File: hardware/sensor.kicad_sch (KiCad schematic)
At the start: 0 parts

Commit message: Alpha 1.0.0 Schematic
First Schematic Version for initial checkup
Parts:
- added C? (x3): 10nF, symbol Device:C
- added C? (x3): 100nF, symbol Device:C
- added R? (x3): 47k, symbol Device:R
- added R? (x3): 91k, symbol Device:R
- added U? (x3): LM321, Package_TO_SOT_SMD:SOT-23-5, symbol Amplifier_Operational:LM321
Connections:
- net 1: now also C?.1, R?.2
- net 2: now also C?.1, R?.2
- net 3: now also C?.1, R?.2
- new net: R?.1, R?.2, U?.1 (+) (x3)
- new net +3V3: C?.1, C?.1, C?.1, U?.5 (V+), U?.5 (V+), U?.5 (V+)
- new net GND: C?.2, C?.2, C?.2, C?.2, C?.2, C?.2, R?.1, R?.1, R?.1, U?.2 (V-), U?.2 (V-), U?.2 (V-), U?.3 (-), U?.3 (-), U?.3 (-), U?.4, U?.4, U?.4
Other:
- note added: "5V to 3V3 signal scaling, noise reduction and Voltage Follower"

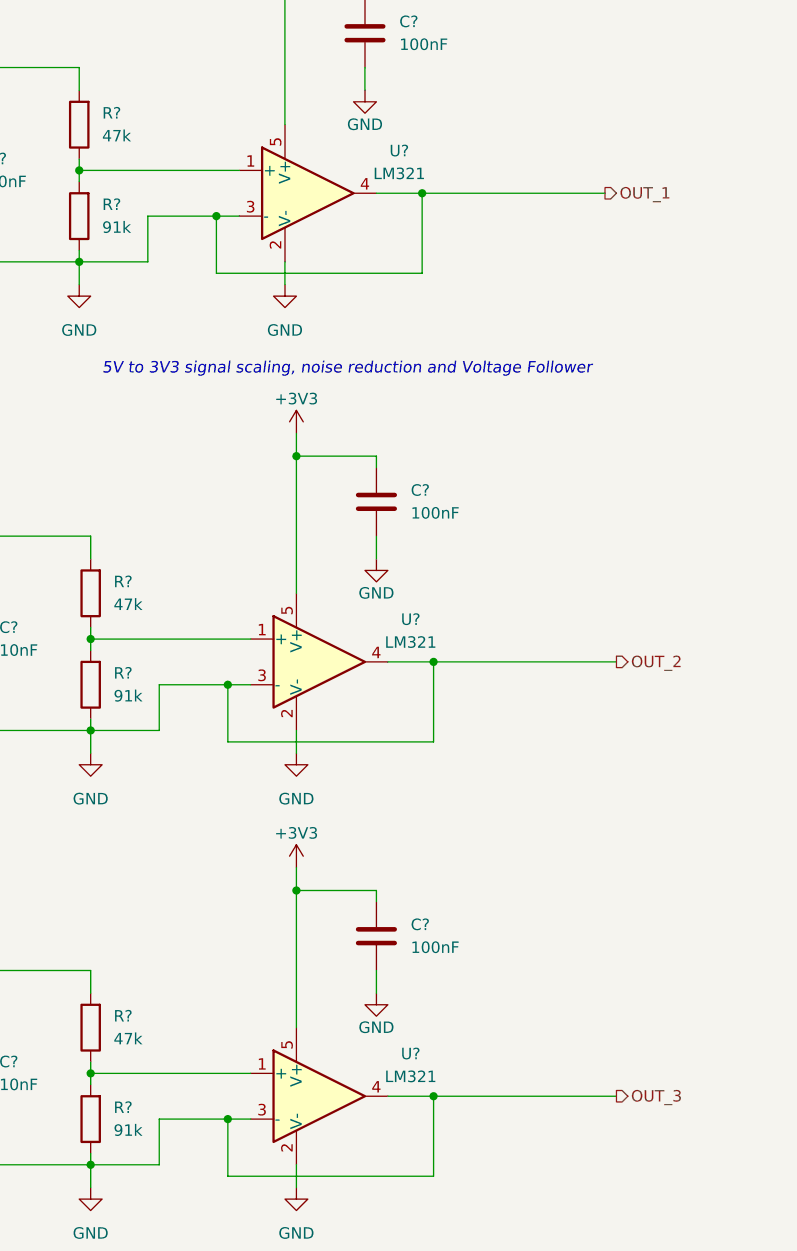
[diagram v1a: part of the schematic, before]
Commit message: Minor changes on v1 schematic
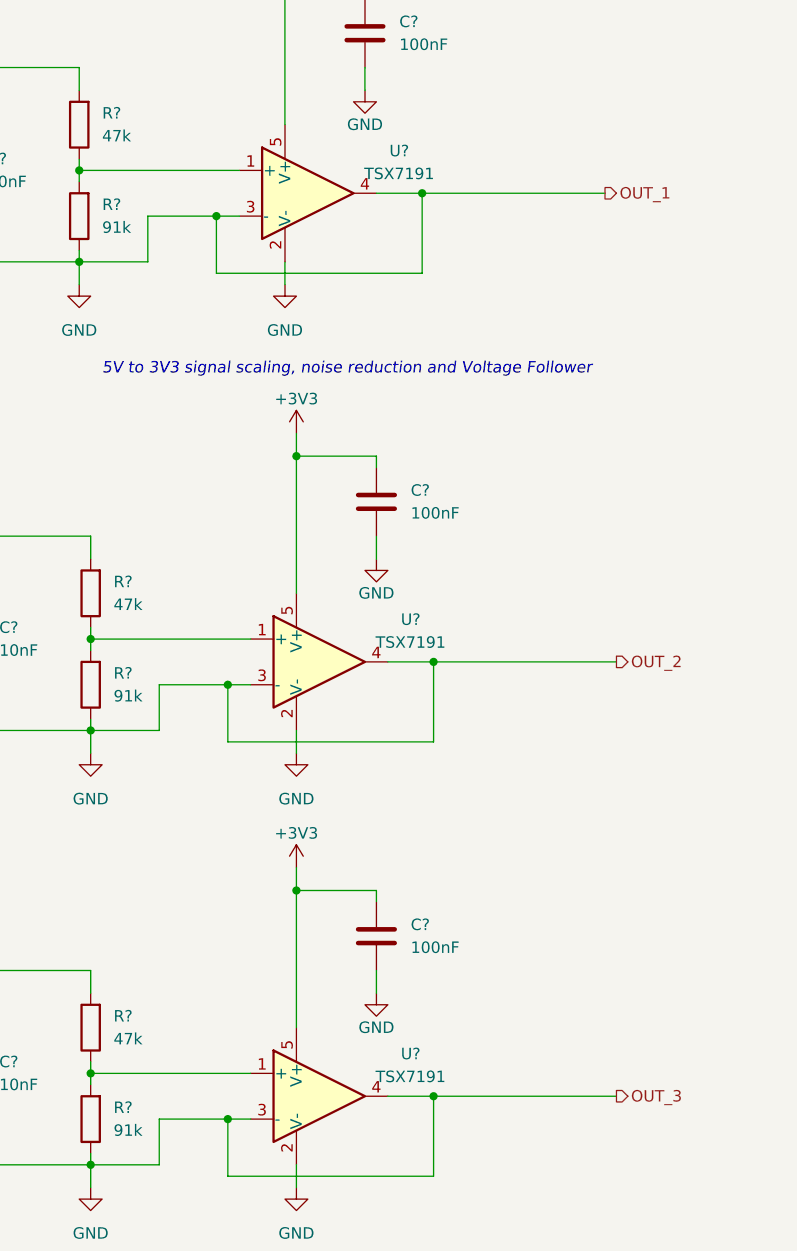
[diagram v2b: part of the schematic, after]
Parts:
- U? (x3): value LM321 -> TSX7191; footprint Package_TO_SOT_SMD:SOT-23-5 -> (none)
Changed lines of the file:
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@@
     (in_bom yes) (on_board yes) (fields_autoplaced)
     (property "Reference" "U?" (id 0) (at 157.48 52.451 0))
-    (property "Value" "LM321" (id 1) (at 157.48 54.991 0))
-    (property "Footprint" "Package_TO_SOT_SMD:SOT-23-5" (id 2) (at 147.32 57.15 0)
-      (effects (font (size 1.27 1.27)) hide)
-    )
-    (property "Datasheet" "http://www.ti.com/lit/ds/symlink/lm321.pdf" (id 3) (at 147.32 57.15 0)
+    (property "Value" "TSX7191" (id 1) (at 157.48 54.991 0))
+    (property "Footprint" "" (id 2) (at 147.32 57.15 0)
+      (effects (font (size 1.27 1.27)) hide)
+    )
+    (property "Datasheet" "" (id 3) (at 147.32 57.15 0)
       (effects (font (size 1.27 1.27)) hide)
     )
@@
     (in_bom yes) (on_board yes) (fields_autoplaced)
     (property "Reference" "U?" (id 0) (at 158.75 104.521 0))
-    (property "Value" "LM321" (id 1) (at 158.75 107.061 0))
-    (property "Footprint" "Package_TO_SOT_SMD:SOT-23-5" (id 2) (at 148.59 109.22 0)
-      (effects (font (size 1.27 1.27)) hide)
-    )
-    (property "Datasheet" "http://www.ti.com/lit/ds/symlink/lm321.pdf" (id 3) (at 148.59 109.22 0)
+    (property "Value" "TSX7191" (id 1) (at 158.75 107.061 0))
+    (property "Footprint" "" (id 2) (at 148.59 109.22 0)
+      (effects (font (size 1.27 1.27)) hide)
+    )
+    (property "Datasheet" "" (id 3) (at 148.59 109.22 0)
       (effects (font (size 1.27 1.27)) hide)
     )
@@
     (in_bom yes) (on_board yes) (fields_autoplaced)
     (property "Reference" "U?" (id 0) (at 158.75 152.781 0))
-    (property "Value" "LM321" (id 1) (at 158.75 155.321 0))
-    (property "Footprint" "Package_TO_SOT_SMD:SOT-23-5" (id 2) (at 148.59 157.48 0)
-      (effects (font (size 1.27 1.27)) hide)
-    )
-    (property "Datasheet" "http://www.ti.com/lit/ds/symlink/lm321.pdf" (id 3) (at 148.59 157.48 0)
-      (effects (font (size 1.27 1.27)) hide)
-    )
+    (property "Value" "TSX7191" (id 1) (at 158.75 155.321 0))
+    (property "Footprint" "" (id 2) (at 148.59 157.48 0)
+      (effects (font (size 1.27 1.27)) hide)
+    )
+    (property "Datasheet" "" (id 3) (at 148.59 157.48 0)
+      (effects (font (size 1.27 1.27)) hide)
+    )

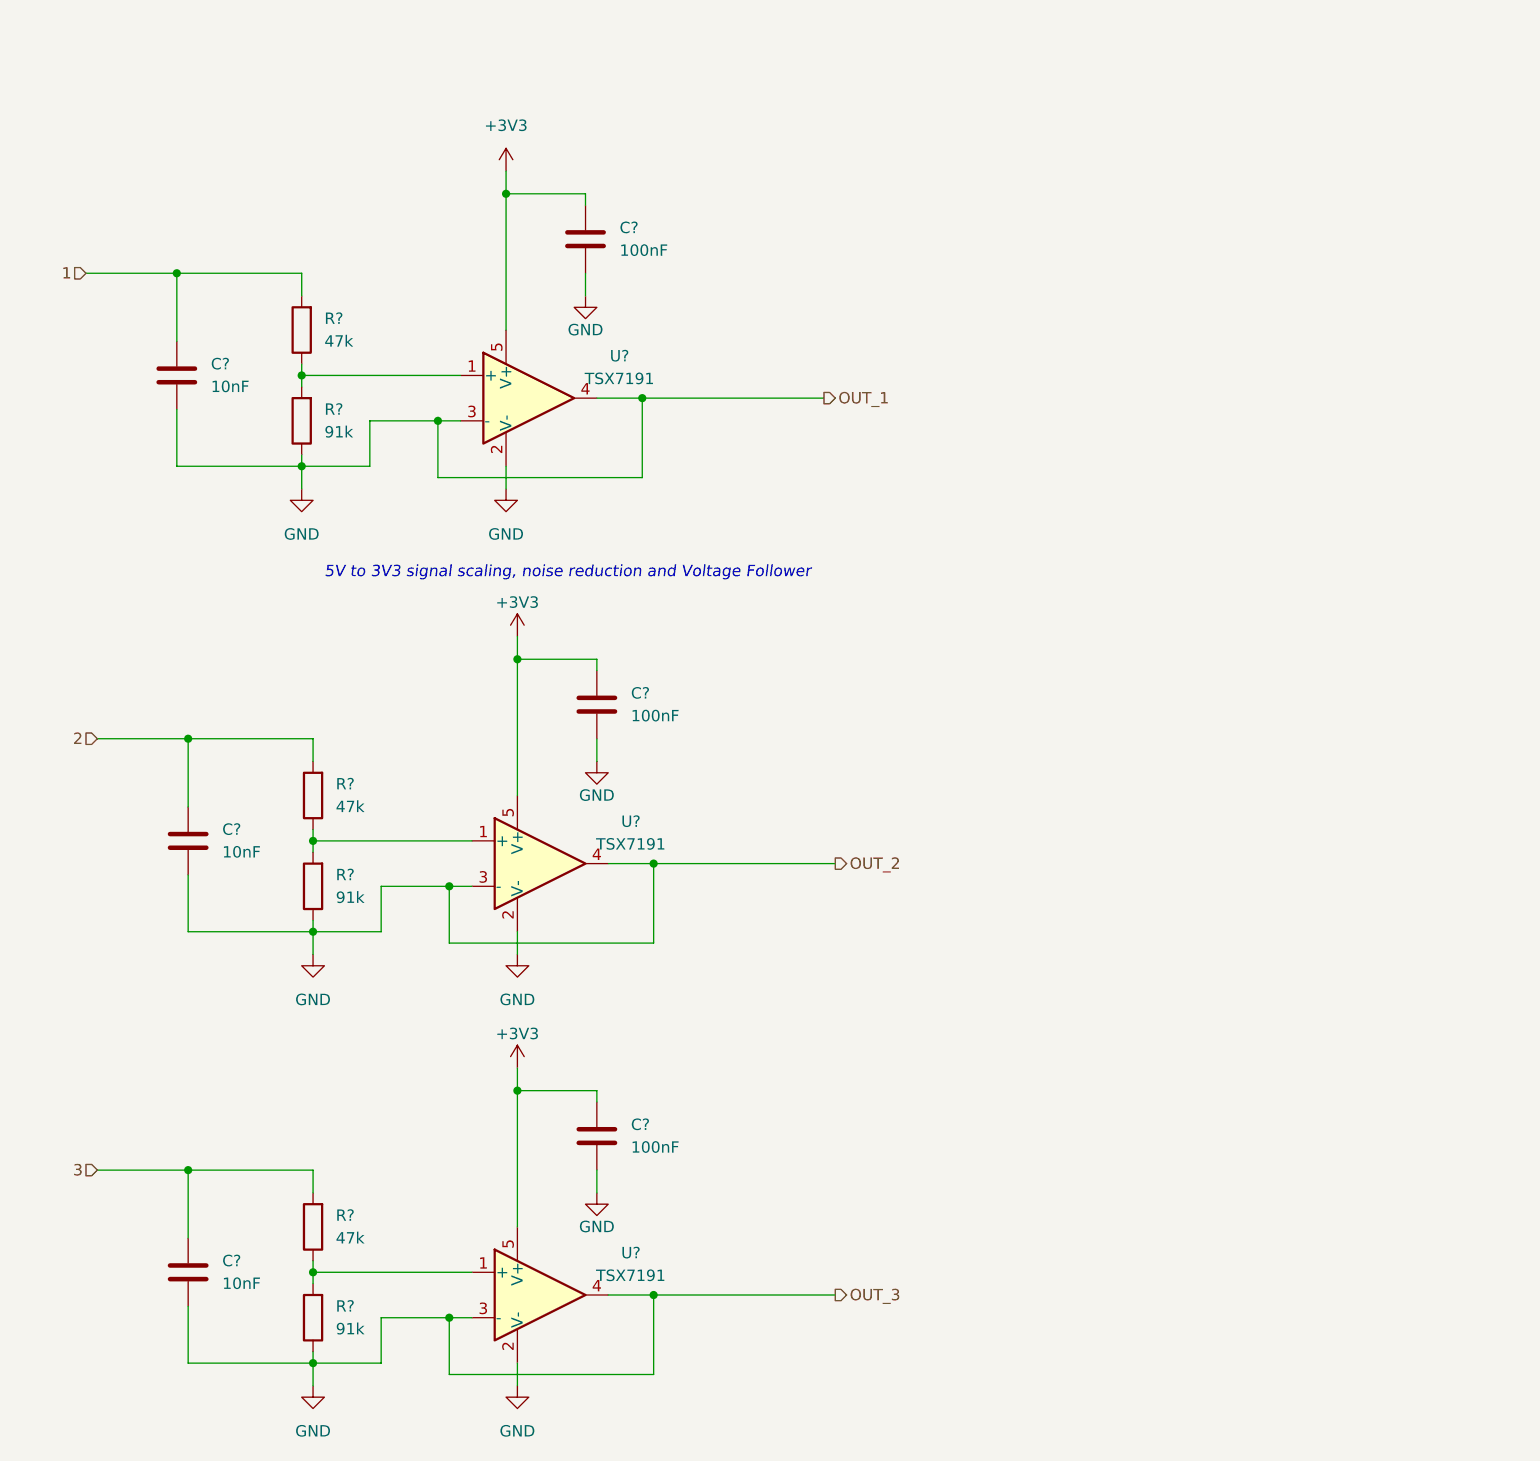
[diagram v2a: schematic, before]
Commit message: minor schematic cleanup
Fixes before second review
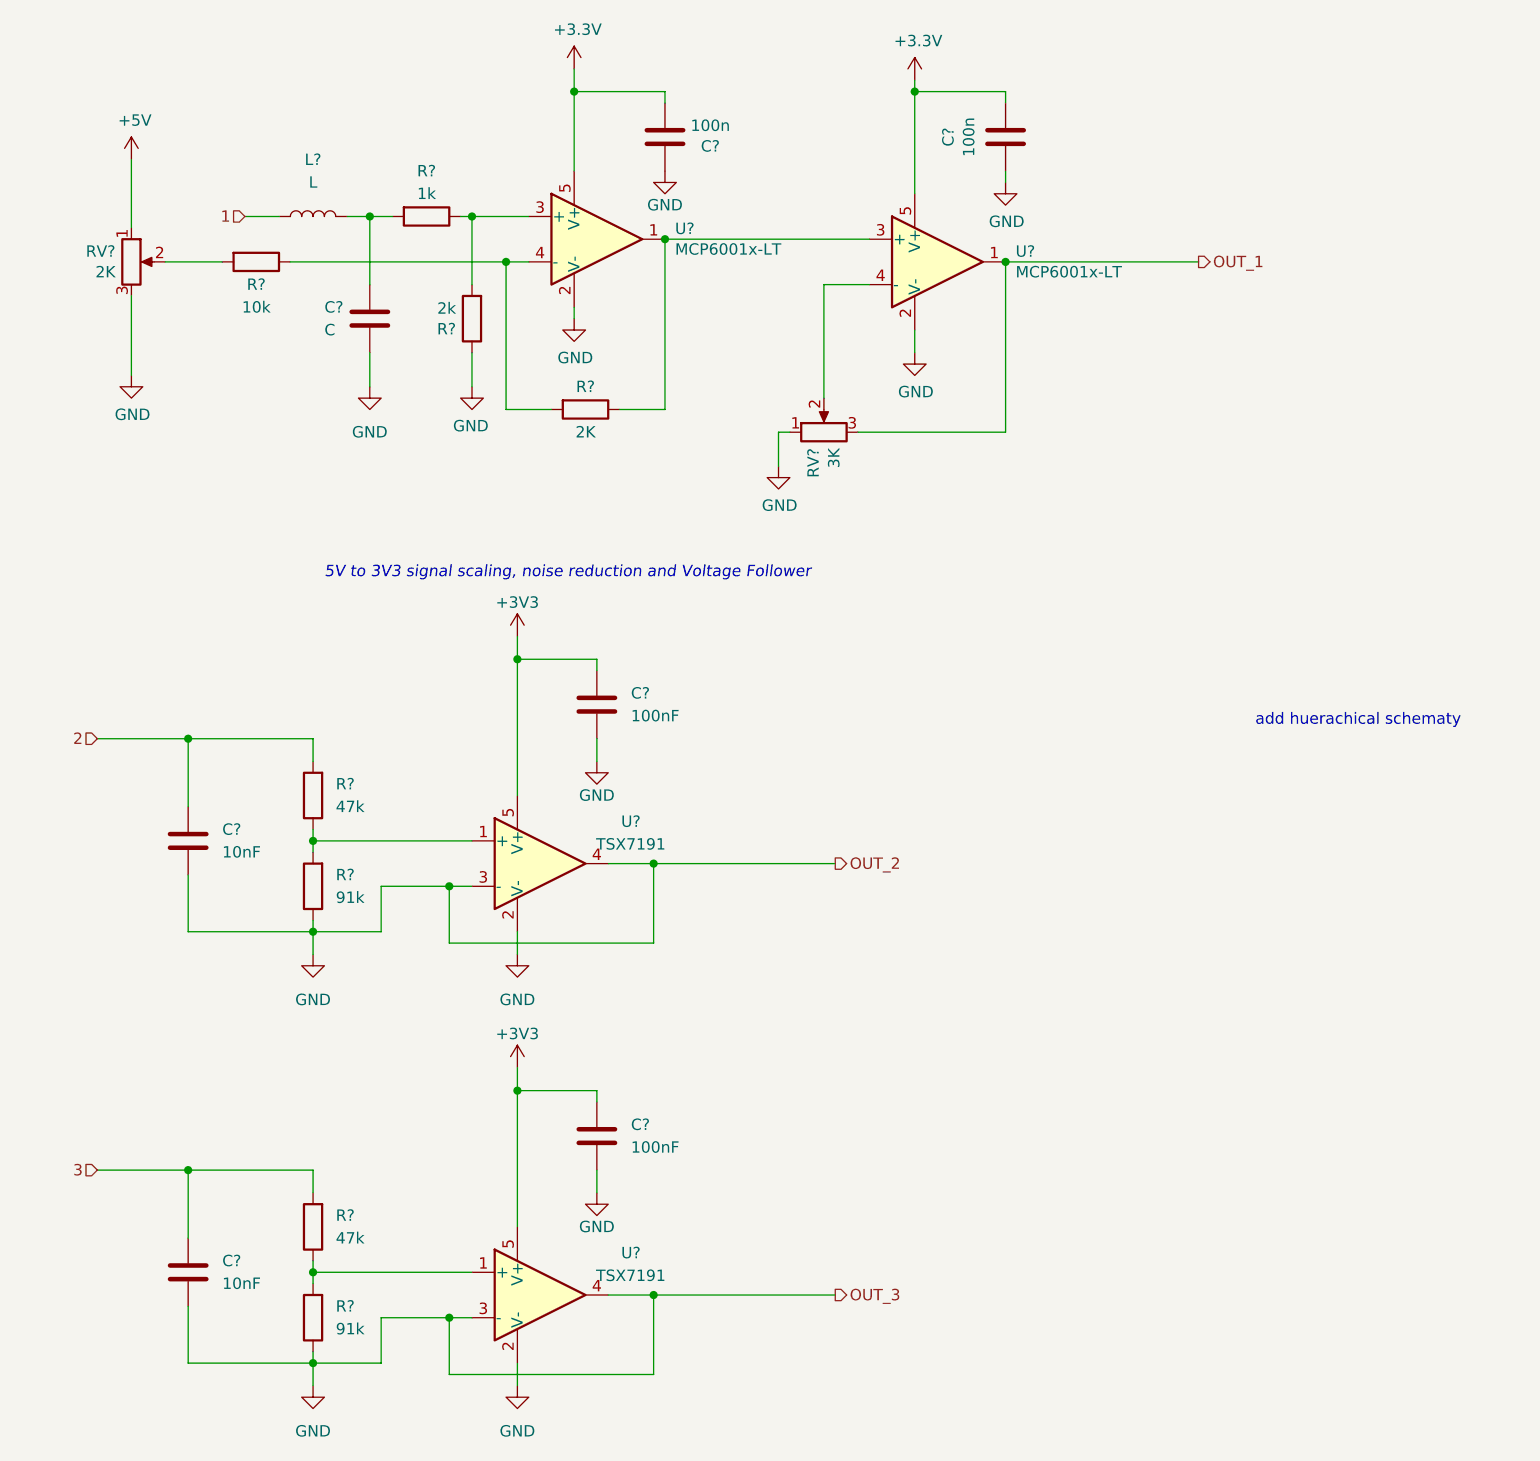
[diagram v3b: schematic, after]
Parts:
- removed C?: 10nF, symbol Device:C
- removed C?: 100nF, symbol Device:C
- removed R?: 47k, symbol Device:R
- removed R?: 91k, symbol Device:R
- removed U?: TSX7191, symbol Amplifier_Operational:LM321
- added C?: C, symbol Device:C
- added C? (x2): 100n, Capacitor_SMD:C_0603_1608Metric, symbol Device:C
- added L?: L, symbol Device:L
- added R?: 2k, Resistor_SMD:R_0603_1608Metric, symbol Device:R
- added R?: 10k, Resistor_SMD:R_0603_1608Metric, symbol Device:R
- added R?: 2K, Resistor_SMD:R_0603_1608Metric, symbol Device:R
- added R?: 1k, Resistor_SMD:R_0603_1608Metric, symbol Device:R
- added RV?: 3K, TC33X-2-103E:TRIM_TC33X-2-103E, symbol karta_pomiarowa_v2-rescue:R_POT-Device
- added RV?: 2K, TC33X-2-103E:TRIM_TC33X-2-103E, symbol karta_pomiarowa_v2-rescue:R_POT-Device
- added U? (x2): MCP6001x-LT, Package_TO_SOT_SMD:SOT-353_SC-70-5, symbol Amplifier_Operational:MCP6001x-LT
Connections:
- net +3V3: now also C?.1, C?.1, U?.5 (V+), U?.5 (V+)
- net 1: now also L?.1
- net GND: now also C?.2, C?.2, C?.2, R?.1, RV?.1, RV?.3, U?.2 (V-), U?.2 (V-)
- new net: C?.1, L?.2, R?.2
- new net: R?.1, R?.2, U?.3 (+)
- new net: RV?.2, U?.4 (-)
- new net: R?.1, U?.1, U?.3 (+)
- new net: R?.1, R?.2, U?.4 (-)
- new net: R?.2, RV?.2
- new net +5V: RV?.1
- new net OUT_1: RV?.3, U?.1
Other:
- note added: "add huerachical schematy"
